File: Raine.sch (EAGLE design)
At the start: 171 parts, among them J1 USB-C-M12-TYPE-C-31-M12, SW1 TL3342F160QG/TR, U2 ATMEGA32U4-AUR44ML-L

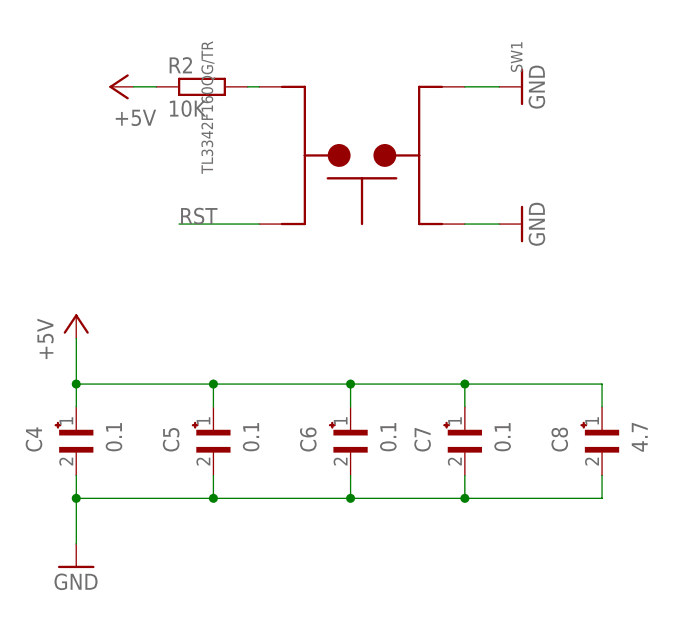
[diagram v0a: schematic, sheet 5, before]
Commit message: Add reset switch to bottom of pcb
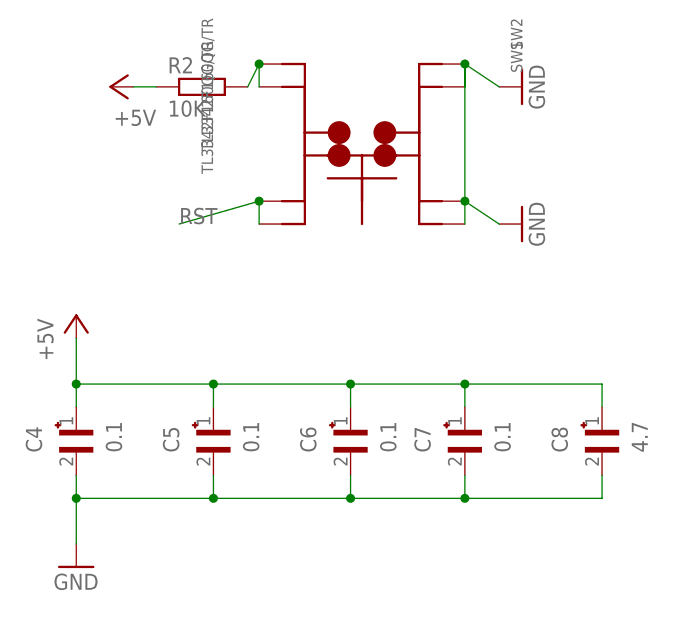
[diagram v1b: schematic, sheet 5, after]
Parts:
- added SW2: TL3342F160QG/TR, Keyboard_parts:TL3342F160QG/TR
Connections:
- net GND: now also SW2.3, SW2.4
- net N$89: now also SW2.1
- net RST: now also SW2.2
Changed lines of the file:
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@@
 <?xml version="1.0" encoding="utf-8"?>
 <!DOCTYPE eagle SYSTEM "eagle.dtd">
-<eagle version="9.4.2">
+<eagle version="9.6.2">
 <drawing>
 <settings>
@@
 <part name="R6" library="Keyboard_parts" library_urn="urn:adsk.eagle:library:6380734" deviceset="R0603" device="" package3d_urn="urn:adsk.eagle:package:6154640/2" value="22"/>
 <part name="GND1" library="supply1" library_urn="urn:adsk.eagle:library:371" deviceset="GND" device=""/>
+<part name="SW2" library="Keyboard_parts" library_urn="urn:adsk.eagle:library:6380734" deviceset="TL3342F160QG/TR" device="" package3d_urn="urn:adsk.eagle:package:6174039/2" value="TL3342F160QG/TR"/>
 </parts>
 <sheets>
@@
 <attribute name="VALUE" x="35.56" y="-2.54" size="1.778" layer="96"/>
 </instance>
+<instance part="SW2" gate="G$1" x="69.85" y="48.26" smashed="yes" rot="R270">
+<attribute name="NAME" x="86.3981" y="60.9892" size="1.27291875" layer="95" rot="R270"/>
+<attribute name="VALUE" x="52.0244" y="60.9926" size="1.273259375" layer="96" rot="R270"/>
+</instance>
 </instances>
 <busses>
@@
 <pinref part="R2" gate="G$1" pin="2"/>
 <pinref part="SW1" gate="G$1" pin="1"/>
-<wire x1="57.15" y1="53.34" x2="58.42" y2="53.34" width="0.1524" layer="91"/>
+<wire x1="57.15" y1="53.34" x2="58.42" y2="55.88" width="0.1524" layer="91"/>
+<pinref part="SW2" gate="G$1" pin="1"/>
+<junction x="58.42" y="55.88"/>
+<wire x1="58.42" y1="55.88" x2="58.42" y2="53.34" width="0.1524" layer="91"/>
 </segment>
 </net>
@@
 <segment>
 <pinref part="SW1" gate="G$1" pin="2"/>
-<wire x1="58.42" y1="38.1" x2="49.53" y2="38.1" width="0.1524" layer="91"/>
+<wire x1="58.42" y1="40.64" x2="49.53" y2="38.1" width="0.1524" layer="91"/>
 <label x="49.53" y="38.1" size="1.778" layer="95"/>
+<pinref part="SW2" gate="G$1" pin="2"/>
+<junction x="58.42" y="40.64"/>
+<wire x1="58.42" y1="40.64" x2="58.42" y2="38.1" width="0.1524" layer="91"/>
 </segment>
 </net>
@@
 <pinref part="SW1" gate="G$1" pin="3"/>
 <pinref part="GND9" gate="1" pin="GND"/>
-<wire x1="81.28" y1="53.34" x2="85.09" y2="53.34" width="0.1524" layer="91"/>
-</segment>
-<segment>
+<wire x1="81.28" y1="55.88" x2="85.09" y2="53.34" width="0.1524" layer="91"/>
+<pinref part="SW2" gate="G$1" pin="3"/>
+<junction x="81.28" y="55.88"/>
+<wire x1="81.28" y1="55.88" x2="81.28" y2="53.34" width="0.1524" layer="91"/>
 <pinref part="GND10" gate="1" pin="GND"/>
 <pinref part="SW1" gate="G$1" pin="4"/>
-<wire x1="85.09" y1="38.1" x2="81.28" y2="38.1" width="0.1524" layer="91"/>
-</segment>
-<segment>
+<wire x1="85.09" y1="38.1" x2="81.28" y2="40.64" width="0.1524" layer="91"/>
+<pinref part="SW2" gate="G$1" pin="4"/>
+<junction x="81.28" y="40.64"/>
+<wire x1="81.28" y1="40.64" x2="81.28" y2="38.1" width="0.1524" layer="91"/>
+<wire x1="81.28" y1="55.88" x2="81.28" y2="40.64" width="0.1524" layer="91"/>
+</segment>
+<segment>
